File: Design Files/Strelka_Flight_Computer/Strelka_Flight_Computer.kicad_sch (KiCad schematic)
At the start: 4 parts

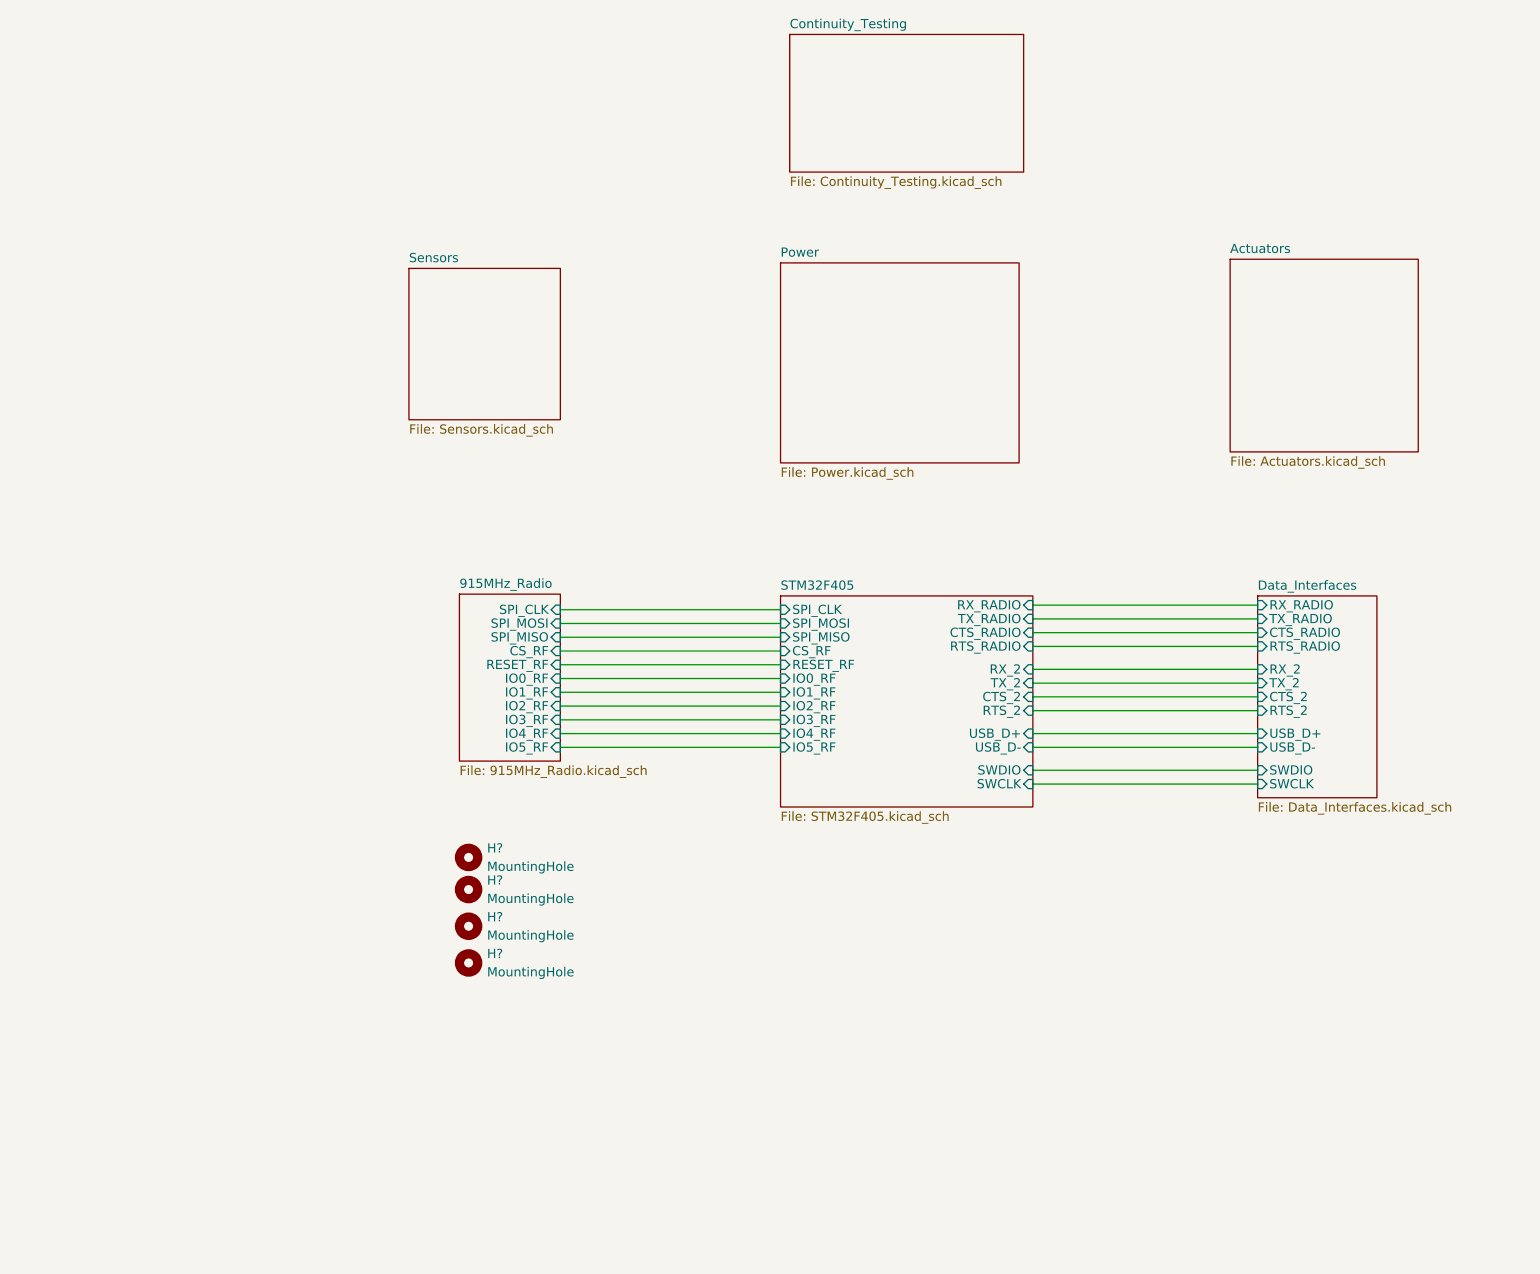
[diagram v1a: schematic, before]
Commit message: Added sensors
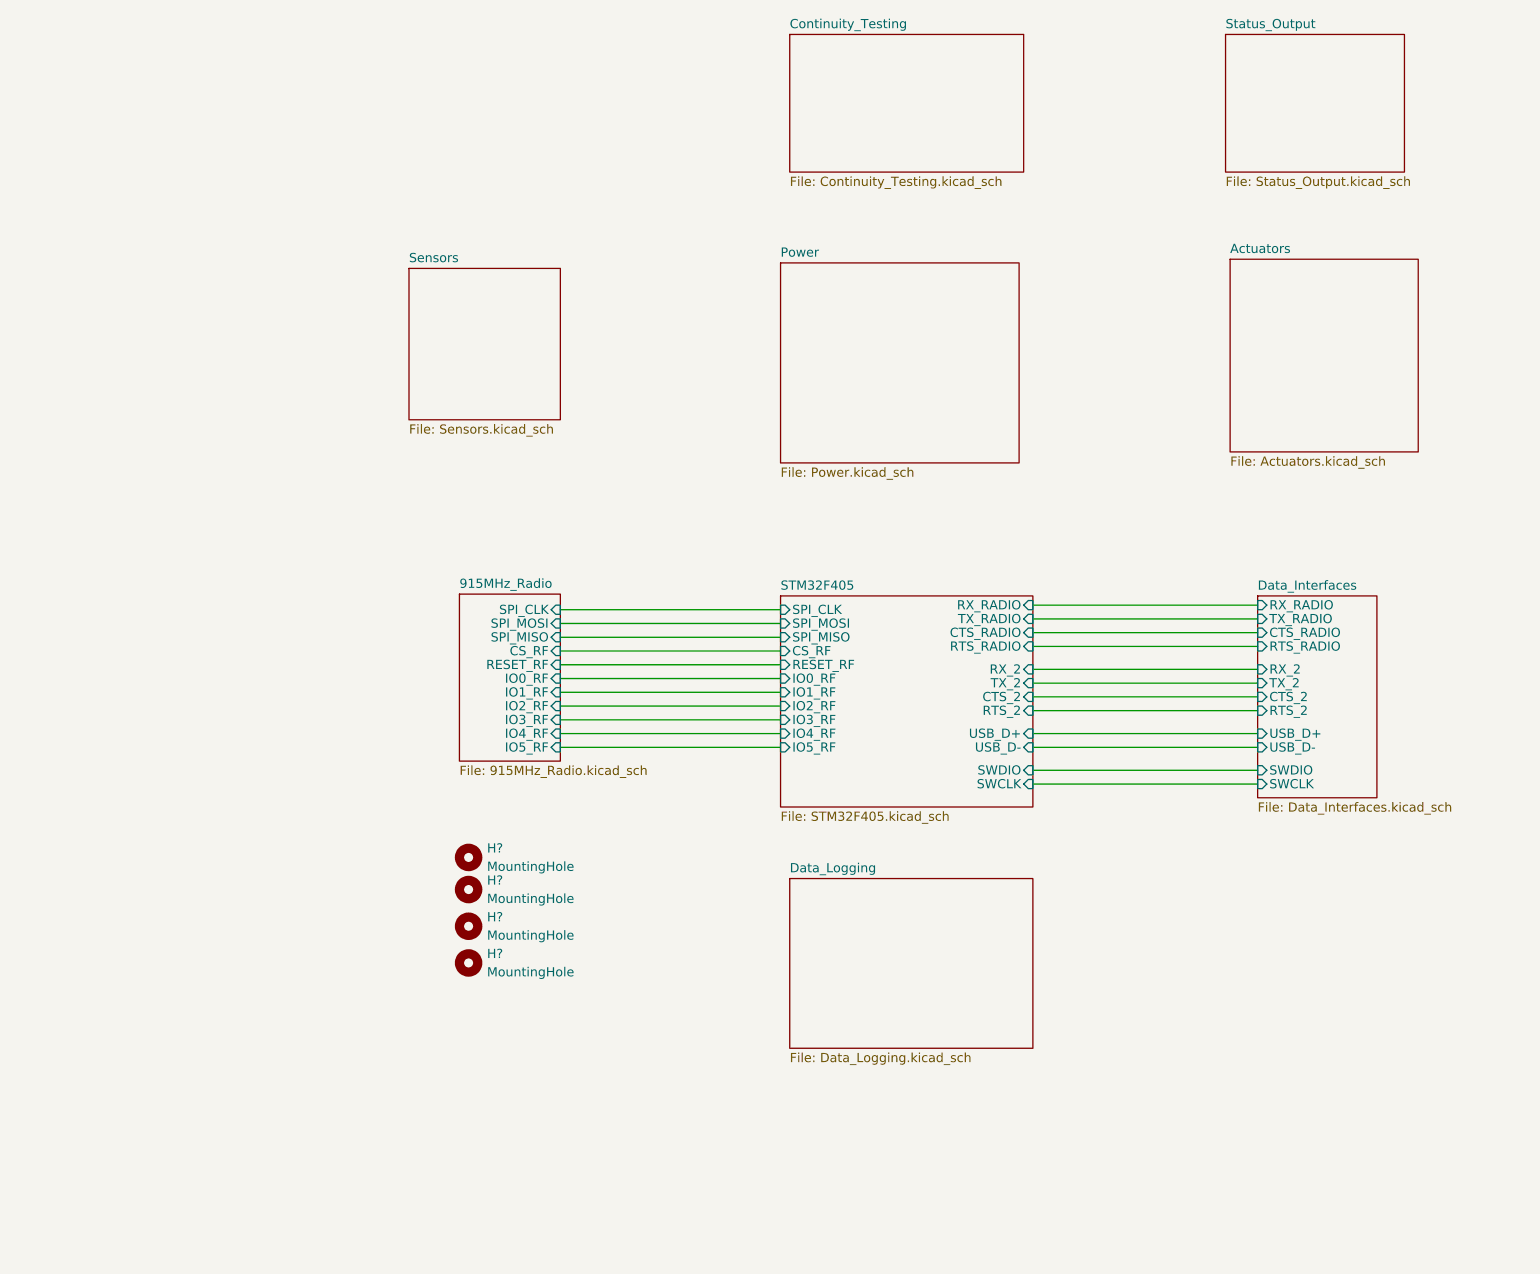
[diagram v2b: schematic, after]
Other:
- added sheet Data_Logging (Data_Logging.kicad_sch)
- added sheet Status_Output (Status_Output.kicad_sch)

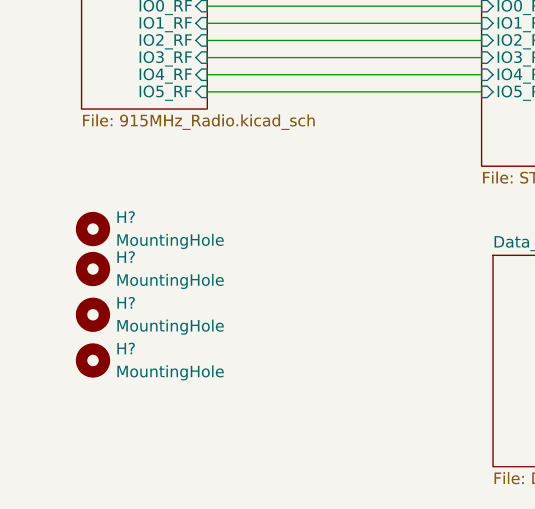
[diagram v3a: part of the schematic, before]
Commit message: Working SPICE sim for ematch continuity circuit
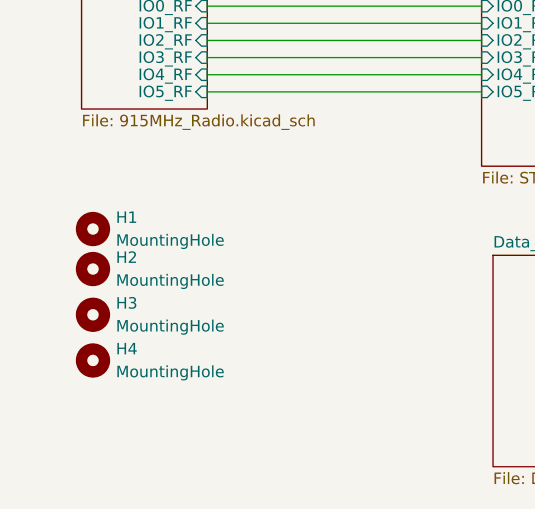
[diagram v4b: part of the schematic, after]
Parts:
- gave numbers to parts that had none: 4

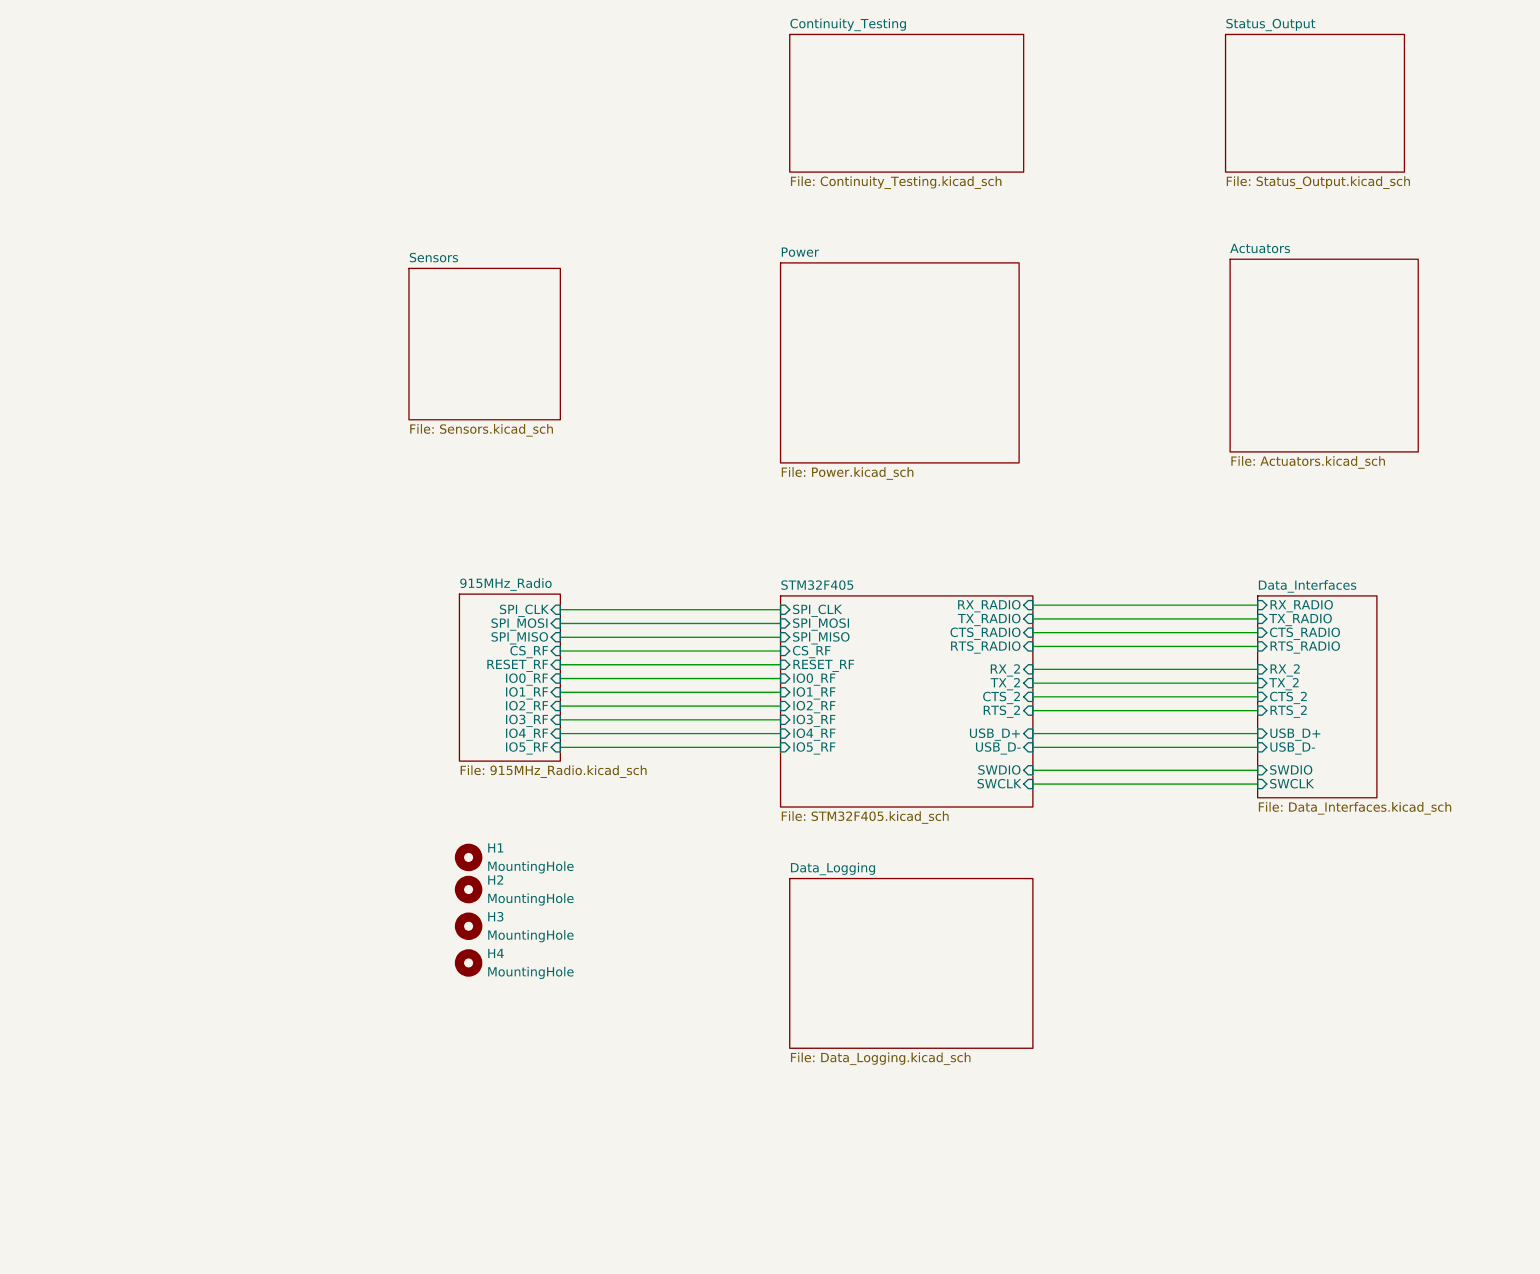
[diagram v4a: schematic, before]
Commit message: Added power board, almost finished Strelka schematic
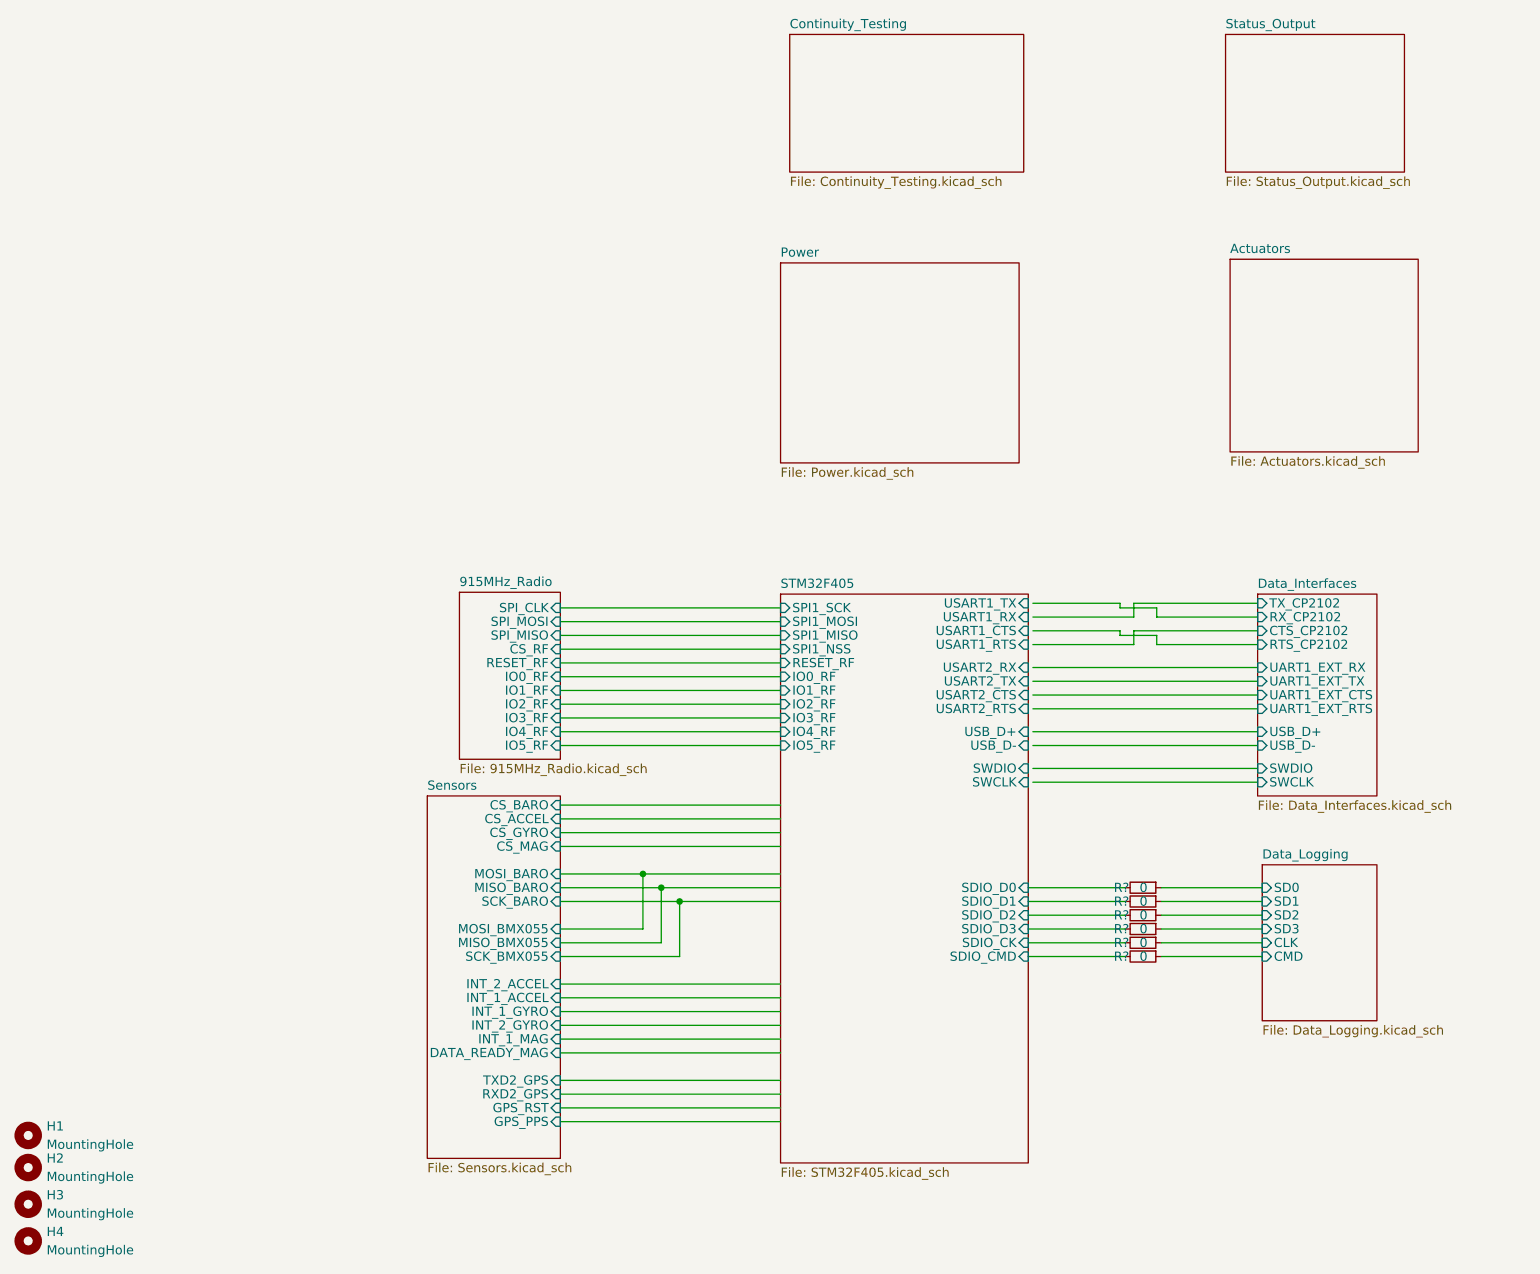
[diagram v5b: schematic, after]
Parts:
- added R? (x6): 0, Resistor_SMD:R_0603_1608Metric_Pad0.98x0.95mm_HandSolder, symbol Device:R_Small
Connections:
- new net Data_Logging/CLK: R?.1
- new net Data_Logging/CMD: R?.1
- new net Data_Logging/SD0: R?.1
- new net Data_Logging/SD1: R?.1
- new net Data_Logging/SD2: R?.1
- new net Data_Logging/SD3: R?.1
- new net STM32F405/SDIO_CK: R?.2
- new net STM32F405/SDIO_CMD: R?.2
- new net STM32F405/SDIO_D0: R?.2
- new net STM32F405/SDIO_D1: R?.2
- new net STM32F405/SDIO_D2: R?.2
- new net STM32F405/SDIO_D3: R?.2
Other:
- sheet Data_Interfaces ports: added CTS_CP2102, RTS_CP2102, RX_CP2102, TX_CP2102, UART1_EXT_CTS, UART1_EXT_RTS, UART1_EXT_RX, UART1_EXT_TX; removed CTS_2, CTS_RADIO, RTS_2, RTS_RADIO, RX_2, RX_RADIO, TX_2, TX_RADIO
- sheet Data_Logging ports: added CLK, CMD, SD0, SD1, SD2, SD3; removed none
- sheet STM32F405 ports: added SDIO_CK, SDIO_CMD, SDIO_D0, SDIO_D1, SDIO_D2, SDIO_D3, SPI1_MISO, SPI1_MOSI, SPI1_NSS, SPI1_SCK, USART1_CTS, USART1_RTS, USART1_RX, USART1_TX, USART2_CTS, USART2_RTS, USART2_RX, USART2_TX; removed CS_RF, CTS_2, CTS_RADIO, RTS_2, RTS_RADIO, RX_2, RX_RADIO, SPI_CLK, SPI_MISO, SPI_MOSI, TX_2, TX_RADIO
- sheet Sensors ports: added CS_ACCEL, CS_BARO, CS_GYRO, CS_MAG, DATA_READY_MAG, GPS_PPS, GPS_RST, INT_1_ACCEL, INT_1_GYRO, INT_1_MAG, INT_2_ACCEL, INT_2_GYRO, MISO_BARO, MISO_BMX055, MOSI_BARO, MOSI_BMX055, RXD2_GPS, SCK_BARO, SCK_BMX055, TXD2_GPS; removed none
- moved on the sheet: H1, H2, H3, H4
